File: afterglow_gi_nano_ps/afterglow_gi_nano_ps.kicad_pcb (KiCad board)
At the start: 2 copper layers, 69 x 118.5 mm, 58 parts, among them J1 Conn_02x17_Odd_Even, J119 OUT GI_CONN_J119, J120 OUT GI_WPC_J120, J121 OUT GI_WPC_J121, J2 POWER_CONN, Q1 FQP30N06L, Q2 FQP30N06L, Q3 FQP30N06L, Q4 FQP30N06L, Q5 FQP30N06L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

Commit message: A PCB layout proposal
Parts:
- removed ? (x4): MountingHole_4.3mm_M4_DIN965, Mounting_Holes:MountingHole_4.3mm_M4_DIN965
- added C4: C, Capacitors_THT:C_Rect_L7.0mm_W3.5mm_P5.00mm, F.Cu at (124.8, 38.5)
- added C5: CP, Capacitors_THT:CP_Radial_D18.0mm_P7.50mm, F.Cu at (129.7, 70.2)
- added C6: CP, Capacitors_THT:CP_Radial_D18.0mm_P7.50mm, F.Cu at (129.8, 109.0)
- added C7: CP, Capacitors_THT:CP_Radial_D18.0mm_P7.50mm, F.Cu at (129.9, 128.4)
- added C8: CP, Capacitors_THT:CP_Radial_D18.0mm_P7.50mm, F.Cu at (129.7, 89.5)
- added F6: Fuse, Fuse_Holders_and_Fuses:Fuseholder5x20_horiz_open_lateral_Type-II, F.Cu at (136.2, 38.1)
- added J6: Conn_01x12_Male, Connectors_Molex:Molex_KK-41791-12_10x3.96mm_Straight, F.Cu at (60.5, 25.1)
- added Q6: FQP30N06L, TO_SOT_Packages_THT:TO-220_Vertical, F.Cu at (113.8, 27.4)
- added Q7: FQP30N06L, TO_SOT_Packages_THT:TO-220_Vertical, F.Cu at (127.0, 27.4)
- added Q8: FQP30N06L, TO_SOT_Packages_THT:TO-220_Vertical, F.Cu at (120.4, 27.4)
- added Q9: FQP30N06L, TO_SOT_Packages_THT:TO-220_Vertical, F.Cu at (133.7, 27.4)
- added REF**: MountingHole_4.3mm_M4, Mounting_Holes:MountingHole_4.3mm_M4, F.Cu at (55.0, 15.5)
- added REF**: MountingHole_4.3mm_M4, Mounting_Holes:MountingHole_4.3mm_M4, F.Cu at (134.9, 15.6)
- added REF**: MountingHole_4.3mm_M4, Mounting_Holes:MountingHole_4.3mm_M4, F.Cu at (134.9, 140.9)
- added REF**: MountingHole_4.3mm_M4, Mounting_Holes:MountingHole_4.3mm_M4, F.Cu at (55.0, 141.0)
- added U3: LT4320_CAP, Housings_DIP:DIP-8_W7.62mm_LongPads, F.Cu at (118.7, 46.4)
- J3: renamed from J120 OUT
- J4: renamed from J121 OUT
- J5: renamed from J119 OUT
- moved afterglow 2.95 mm to (52.5, 109.5)
- moved FLAKIE 0.67 mm to (91.8, 34.4)
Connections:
- net Net-(C2-Pad1) renamed /OUT_DC
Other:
- board size 69 x 118.5 mm -> 89 x 134.5 mm
- board text added: "(c) 2020 by bitfield labs"
- board text added: "v1.1"
- board text removed: "(c) 2019 by morbid cornflakes"
- board text removed: "v1.0"

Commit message: Some progress
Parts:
- moved Q8 27.7 mm to (123.0, 55.0), turned to 180 degrees
- moved Q9 22.3 mm to (123.0, 47.0), turned to 180 degrees
- moved J1 21.2 mm to (132.8, 73.8)
- moved C4 15.4 mm to (109.5, 37.0), turned to 270 degrees
- moved F6 13.9 mm to (129.5, 26.0), turned to 180 degrees
- moved U3 13.0 mm to (112.0, 57.5), turned to 180 degrees
- moved Q7 12.2 mm to (123.0, 39.0), turned to 180 degrees
- moved C5 11.7 mm to (118.0, 69.8)
- moved Q6 10.1 mm to (123.0, 31.5), turned to 180 degrees
- moved C8 0.30 mm to (130.0, 89.5)
- moved C6 0.20 mm to (130.0, 109.0)
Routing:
- net Net-(F6-Pad2): track 0.00 -> 58.7 mm
- net Net-(J6-Pad10): track 0.00 -> 52.0 mm
- net Net-(F6-Pad1): track 0.00 -> 29.8 mm
- net GND: track 387.3 -> 410.9 mm
- net /ZC: track 42.8 -> 65.9 mm, vias 0 -> 1
- net /BLANK: track 21.5 -> 42.6 mm
- net /TRIAC: track 76.4 -> 95.2 mm
- net /D7: track 53.6 -> 72.0 mm
- net /D6: track 39.6 -> 24.3 mm
- net /D5: track 32.9 -> 19.8 mm
- net /D3: track 16.1 -> 4.49 mm
- net /D4: track 26.6 -> 15.7 mm
- net /D0: track 18.6 -> 8.12 mm, vias 1 -> 0
- net /D2: track 15.5 -> 8.38 mm
- net /D1: track 23.4 -> 17.0 mm
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
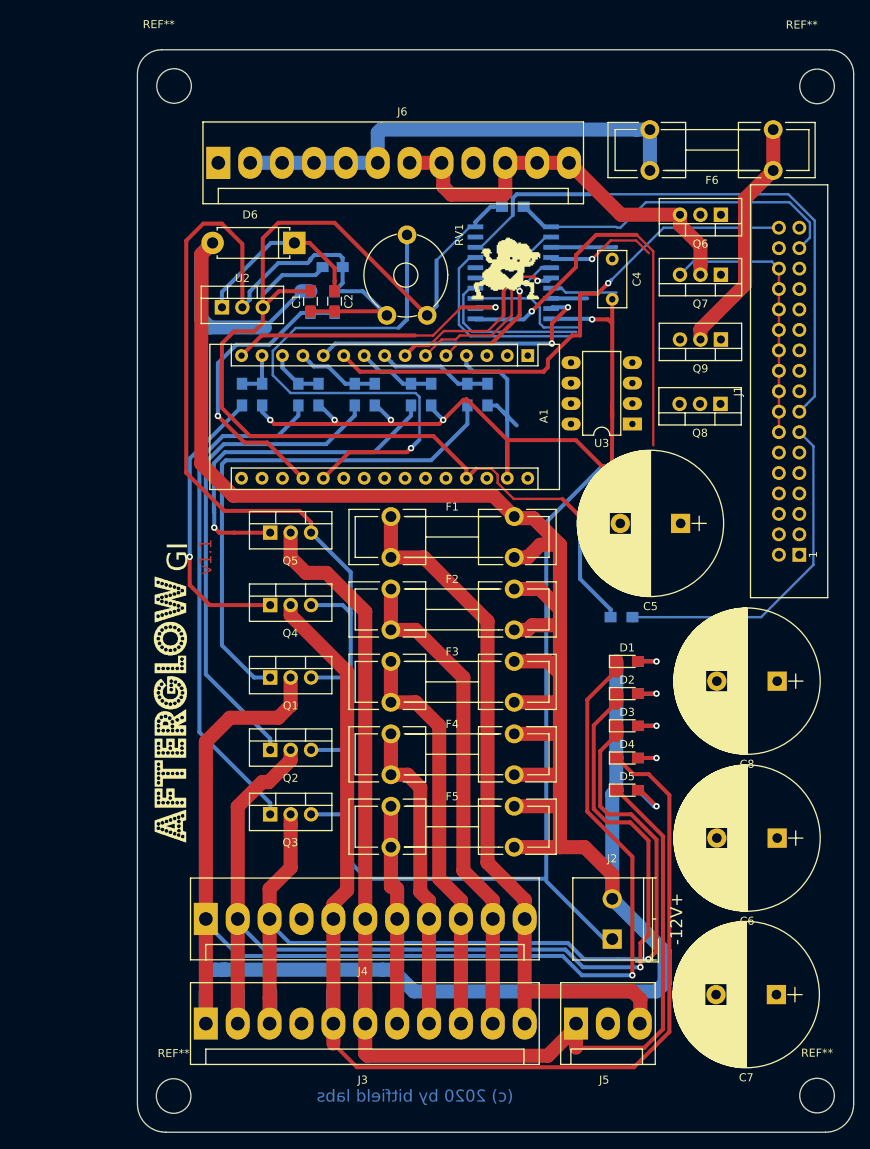
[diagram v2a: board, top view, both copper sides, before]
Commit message: New PCB layout with power supply
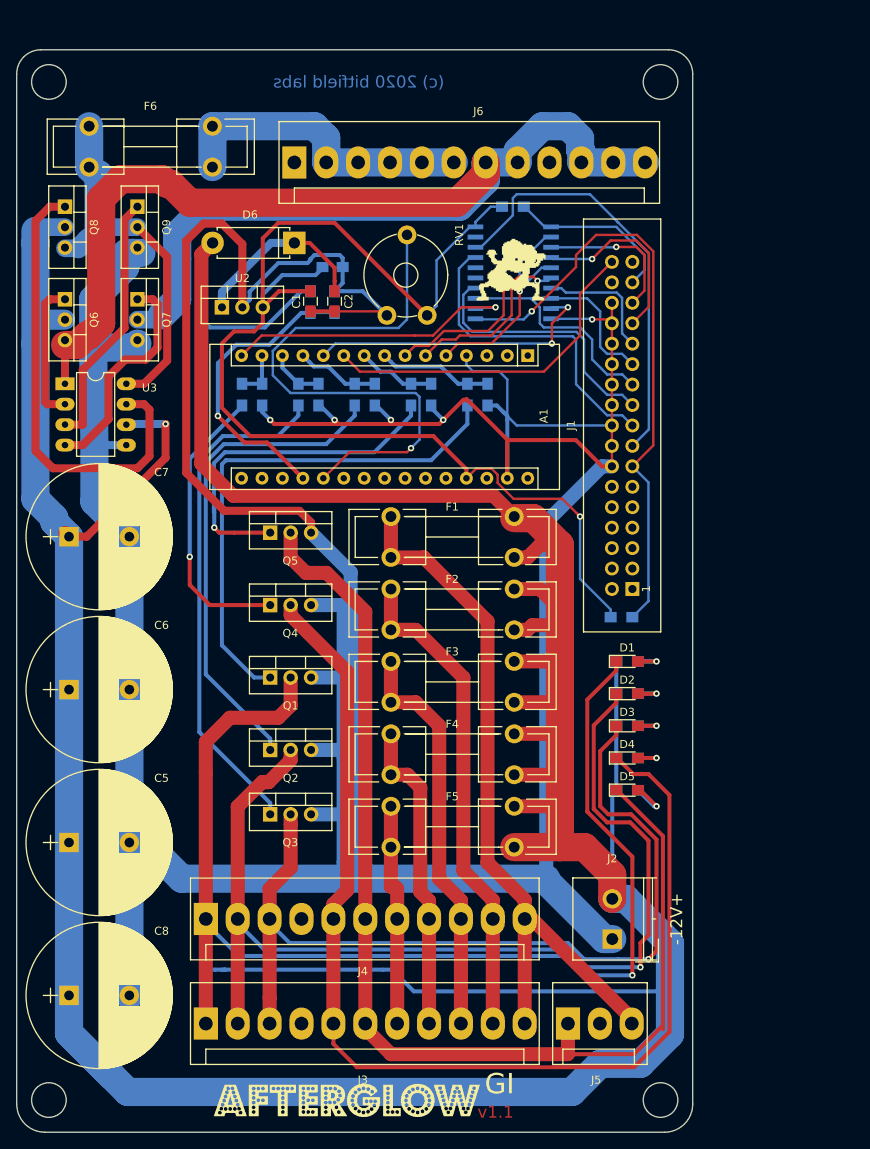
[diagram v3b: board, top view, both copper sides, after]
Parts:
- removed C4: C, Capacitors_THT:C_Rect_L7.0mm_W3.5mm_P5.00mm
- removed REF** (x4): MountingHole_4.3mm_M4, Mounting_Holes:MountingHole_4.3mm_M4
- added ?: MountingHole_4.3mm_M4_DIN965, Mounting_Holes:MountingHole_4.3mm_M4_DIN965, F.Cu at (39.5, 141.5)
- added ?: MountingHole_4.3mm_M4_DIN965, Mounting_Holes:MountingHole_4.3mm_M4_DIN965, F.Cu at (115.5, 141.5)
- added ?: MountingHole_4.3mm_M4_DIN965, Mounting_Holes:MountingHole_4.3mm_M4_DIN965, F.Cu at (39.5, 15.0)
- added ?: MountingHole_4.3mm_M4_DIN965, Mounting_Holes:MountingHole_4.3mm_M4_DIN965, F.Cu at (115.5, 15.0)
- moved C7 104.7 mm to (42.0, 71.5), turned to 0 degrees
- moved C8 96.3 mm to (42.0, 128.5), turned to 0 degrees
- moved C6 89.9 mm to (42.0, 90.5), turned to 0 degrees
- moved C5 85.7 mm to (42.0, 109.5), turned to 0 degrees
- moved F6 85.2 mm to (44.5, 20.5), turned to 0 degrees
- moved Q8 85.1 mm to (41.5, 30.5), turned to 270 degrees
- moved Q6 82.2 mm to (41.5, 42.0), turned to 270 degrees
- moved Q9 74.4 mm to (50.5, 30.5), turned to 270 degrees
- moved Q7 72.6 mm to (50.5, 42.0), turned to 270 degrees
- moved U3 70.7 mm to (41.5, 52.5), turned to 0 degrees
- moved afterglow 30.9 mm to (60.0, 139.5), turned to 0 degrees
- moved J1 21.2 mm to (112.0, 78.0)
- moved J6 9.45 mm to (70.0, 25.0)
- moved J5 1.00 mm to (104.0, 132.0)
- moved FLAKIE 0.67 mm to (92.5, 34.5)
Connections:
- C2 pad 1: /OUT_DC -> Net-(C2-Pad1)
- C5 pad 1: /OUT_DC -> +12V
- C6 pad 1: /OUT_DC -> +12V
- C7 pad 1: /OUT_DC -> +12V
- C8 pad 1: /OUT_DC -> +12V
- D6 pad 1: /OUT_DC -> Net-(C2-Pad1)
- Q6 pad 2: /OUT_DC -> +12V
- Q8 pad 2: /OUT_DC -> +12V
- U2 pad 1: /OUT_DC -> Net-(C2-Pad1)
- U3 pad 6: /OUT_DC -> +12V
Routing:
- net +12V: track 307.3 -> 551.1 mm, vias 0 -> 1
- net GND: track 410.9 -> 526.3 mm
- net Net-(J6-Pad10): track 52.0 -> 162.9 mm
- net Net-(Q8-Pad1): track 0.00 -> 57.6 mm
- net Net-(Q9-Pad1): track 0.00 -> 32.1 mm
- net Net-(Q7-Pad1): track 0.00 -> 27.8 mm
- net /ZC: track 65.9 -> 42.8 mm, vias 1 -> 0
- net Net-(C2-Pad1): track 0.00 -> 22.6 mm
- net /OUT_DC: track 22.6 -> 0.00 mm
- net /BLANK: track 42.6 -> 21.5 mm
- net Net-(F6-Pad2): track 58.7 -> 38.7 mm
- net Net-(F6-Pad1): track 29.8 -> 48.8 mm
- net /TRIAC: track 95.2 -> 76.4 mm
- net /D7: track 72.0 -> 53.6 mm
- net Net-(Q6-Pad1): track 0.00 -> 17.5 mm
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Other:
- board size 89 x 134.5 mm -> 84 x 134.5 mm
- net class Default: clearance 0.3 -> 0.2
- rule trace_clearance: 0.3 -> 0.2
- board text added: "(c) 2020 bitfield labs"
- board text removed: "(c) 2020 by bitfield labs"
